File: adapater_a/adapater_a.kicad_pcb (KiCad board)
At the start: 2 copper layers, 68.6 x 53.3 mm, 8 parts, among them J1 Power, J2 Digital/PWM, J3 Analog, J4 Digital/PWM

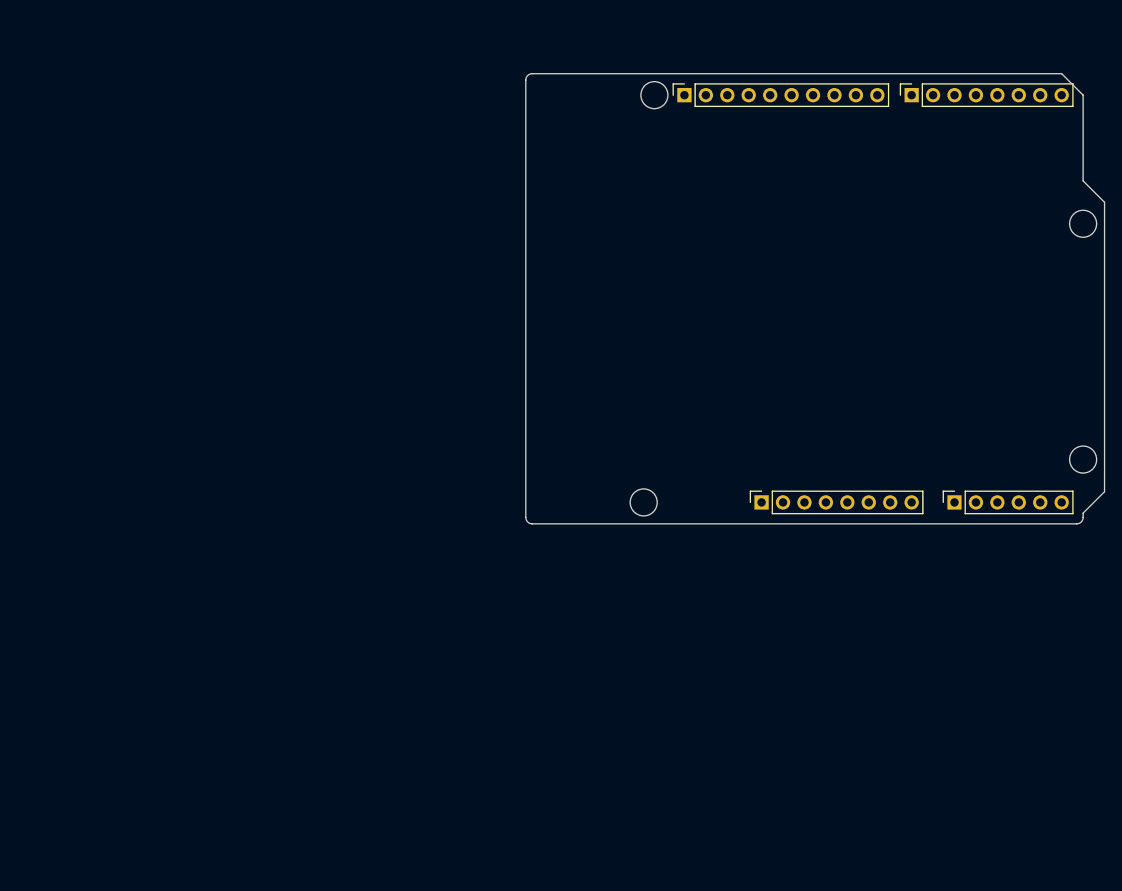
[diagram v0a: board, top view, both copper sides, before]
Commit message: Add first version of adpater A
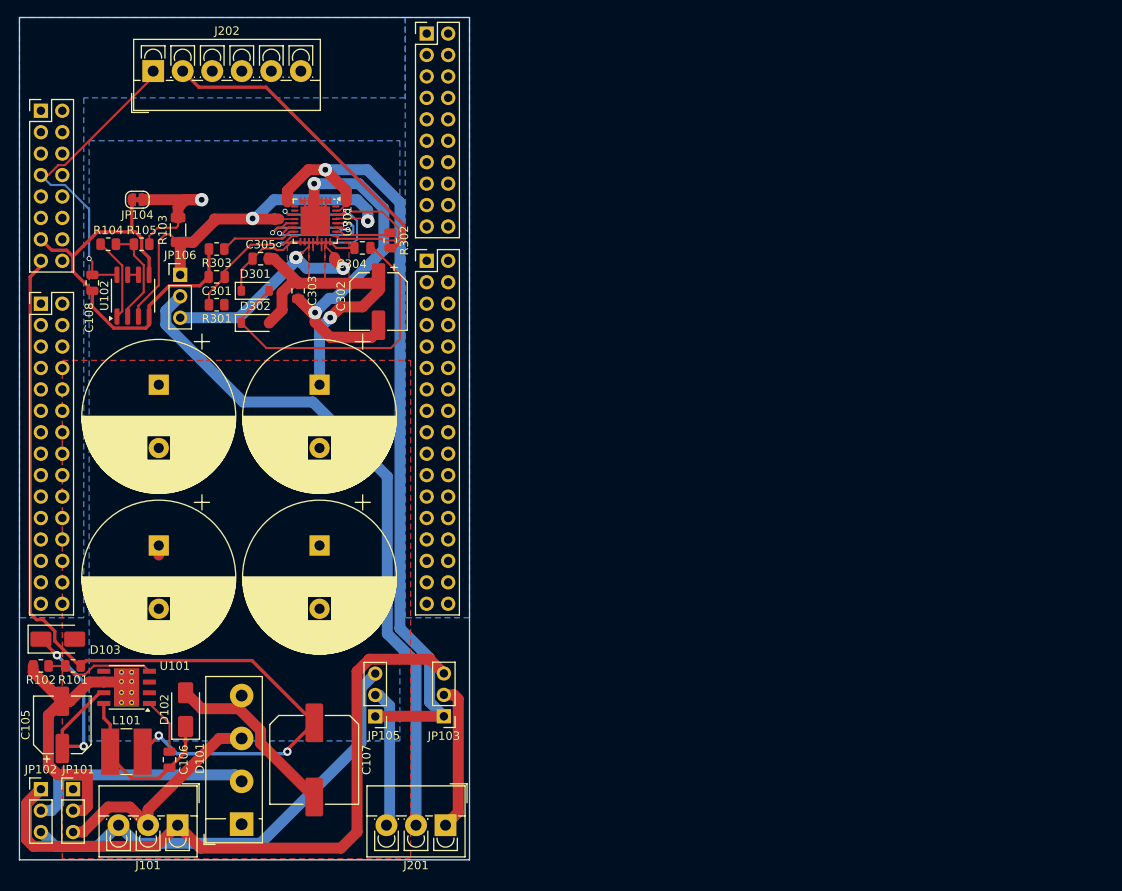
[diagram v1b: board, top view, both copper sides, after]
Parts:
- removed J1: Power, Connector_PinSocket_2.54mm:PinSocket_1x08_P2.54mm_Vertical
- removed J2: Digital/PWM, Connector_PinSocket_2.54mm:PinSocket_1x10_P2.54mm_Vertical
- removed J3: Analog, Connector_PinSocket_2.54mm:PinSocket_1x06_P2.54mm_Vertical
- removed J4: Digital/PWM, Connector_PinSocket_2.54mm:PinSocket_1x08_P2.54mm_Vertical
- removed MH1, MH2, MH3, MH4: MountingHole_3.2mm, Arduino_MountingHole:MountingHole_3.2mm
- added C101: 4m7, Capacitor_THT:CP_Radial_D18.0mm_P7.50mm, F.Cu at (56.5, 102.6)
- added C102: 4m7, Capacitor_THT:CP_Radial_D18.0mm_P7.50mm, F.Cu at (75.6, 102.6)
- added C103: 4m7, Capacitor_THT:CP_Radial_D18.0mm_P7.50mm, F.Cu at (75.6, 83.5)
- added C104: 4m7, Capacitor_THT:CP_Radial_D18.0mm_P7.50mm, F.Cu at (56.5, 83.5)
- added C105: 10u, Capacitor_SMD:CP_Elec_6.3x5.4, F.Cu at (45.1, 123.8)
- added C106: 10n, Capacitor_SMD:C_0805_2012Metric, F.Cu at (57.8, 127.9)
- added C107: 220u, Capacitor_SMD:C_Elec_10x10.2, F.Cu at (74.9, 128.0)
- added C108: 100n, Capacitor_SMD:C_0805_2012Metric, F.Cu at (48.6, 71.4)
- added C301: 5n6, Capacitor_SMD:C_0805_2012Metric, F.Cu at (63.4, 70.7)
- added C302: 100u, Capacitor_SMD:CP_Elec_6.3x5.4, F.Cu at (82.5, 73.7)
- added C303: 100n, Capacitor_SMD:C_0805_2012Metric, F.Cu at (73.0, 72.4)
- added C304: 10n, Capacitor_SMD:C_0805_2012Metric, F.Cu at (80.6, 67.3)
- added C305: 220n, Capacitor_SMD:C_0805_2012Metric, F.Cu at (68.6, 68.6)
- added D101: KBL406, Diode_THT:Diode_Bridge_Vishay_KBL, F.Cu at (66.3, 135.6)
- added D102: B340, Diode_SMD:D_SMA, F.Cu at (59.7, 122.0)
- added D103: B340, Diode_SMD:D_SMA, F.Cu at (44.5, 113.7)
- added D301: 1N4148W, Diode_SMD:D_SOD-123, F.Cu at (67.9, 72.4)
- added D302: 1N4148W, Diode_SMD:D_SOD-123, F.Cu at (67.9, 76.2)
- added J101: Conn_01x03, TerminalBlock_4Ucon:TerminalBlock_4Ucon_1x03_P3.50mm_Vertical, F.Cu at (58.7, 135.7)
- added J102: CN8, Connector_PinHeader_2.54mm:PinHeader_2x08_P2.54mm_Vertical, F.Cu at (42.5, 51.0)
- added J103: CN9, Connector_PinHeader_2.54mm:PinHeader_2x15_P2.54mm_Vertical, F.Cu at (42.5, 73.9)
- added J104: CN7, Connector_PinHeader_2.54mm:PinHeader_2x10_P2.54mm_Vertical, F.Cu at (88.3, 41.9)
- added J105: CN10, Connector_PinHeader_2.54mm:PinHeader_2x17_P2.54mm_Vertical, F.Cu at (88.3, 68.8)
- added J201: Conn_01x03, TerminalBlock_4Ucon:TerminalBlock_4Ucon_1x03_P3.50mm_Vertical, F.Cu at (90.5, 135.7)
- added J202: Conn_01x06, TerminalBlock_4Ucon:TerminalBlock_4Ucon_1x06_P3.50mm_Vertical, F.Cu at (55.8, 46.4)
- added JP101: Jumper_3_Bridged12, Connector_PinHeader_2.54mm:PinHeader_1x03_P2.54mm_Vertical, F.Cu at (46.4, 131.4)
- added JP102: Jumper_3_Bridged12, Connector_PinHeader_2.54mm:PinHeader_1x03_P2.54mm_Vertical, F.Cu at (42.5, 131.4)
- added JP103: Jumper_3_Bridged12, Connector_PinHeader_2.54mm:PinHeader_1x03_P2.54mm_Vertical, F.Cu at (90.3, 122.8)
- added JP104: SolderJumper_2_Bridged, Jumper:SolderJumper-2_P1.3mm_Bridged_RoundedPad1.0x1.5mm, F.Cu at (54.0, 61.6)
- added JP105: Jumper_3_Bridged12, Connector_PinHeader_2.54mm:PinHeader_1x03_P2.54mm_Vertical, F.Cu at (82.2, 122.8)
- added JP106: Jumper_3_Bridged12, Connector_PinHeader_2.54mm:PinHeader_1x03_P2.54mm_Vertical, F.Cu at (59.0, 70.5)
- added L101: 47u, Inductor_SMD:L_Ferrocore_DLG-0504, F.Cu at (52.7, 127.0)
- added R101: 10k, Resistor_SMD:R_0805_2012Metric, F.Cu at (46.4, 116.8)
- added R102: 1k2, Resistor_SMD:R_0805_2012Metric, F.Cu at (42.5, 116.8)
- added R103: 0R1, Resistor_SMD:R_1206_3216Metric, F.Cu at (58.8, 65.2)
- added R104: 68k, Resistor_SMD:R_0805_2012Metric, F.Cu at (50.5, 66.9)
- added R105: 10k, Resistor_SMD:R_0805_2012Metric, F.Cu at (54.5, 66.9)
- added R301: 100k, Resistor_SMD:R_0805_2012Metric, F.Cu at (63.4, 74.0)
- added R302: 5k, Resistor_SMD:R_0805_2012Metric, F.Cu at (83.9, 66.4)
- added R303: 5k, Resistor_SMD:R_0805_2012Metric, F.Cu at (63.4, 67.4)
- added U101: TPS5430DDA, Package_SO:TI_SO-PowerPAD-8_ThermalVias, F.Cu at (52.7, 119.4)
- added U102: TLV2372, Package_SO:SOIC-8_3.9x4.9mm_P1.27mm, F.Cu at (53.5, 73.0)
- added U301: L6226, Package_DFN_QFN:UFQFPN-32-1EP_5x5mm_P0.5mm_EP3.5x3.5mm, F.Cu at (75.1, 64.1)
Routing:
- net GNDPWR: track 0.00 -> 134.2 mm, vias 0 -> 3
- net VCC: track 0.00 -> 105.4 mm, vias 0 -> 2
- net /Driver/V_TRACK: track 0.00 -> 96.0 mm, vias 0 -> 1
- net GND: track 0.00 -> 89.2 mm
- net /V_drive: track 0.00 -> 82.1 mm
- net /Connector/GND_PWR: track 0.00 -> 80.5 mm
- net Net-(U301-ENB): track 0.00 -> 54.5 mm, vias 0 -> 3
- net /V_switch: track 0.00 -> 54.4 mm
- net /Driver/GND_SENSE: track 0.00 -> 52.4 mm, vias 0 -> 2
- net /Driver/V_in: track 0.00 -> 41.1 mm, vias 0 -> 1
- net Net-(D301-A): track 0.00 -> 38.1 mm
- net +3V3: track 0.00 -> 37.0 mm, vias 0 -> 1
- net /Driver/GND_TRACK: track 0.00 -> 30.6 mm, vias 0 -> 2
- net Net-(JP102-C): track 0.00 -> 27.6 mm
- net /GND_PWR: track 0.00 -> 27.4 mm
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- added copper zone on F.Cu, net /Driver/GND_TRACK
- added copper zone on F.Cu, net /Driver/V_in
- added copper zone on B.Cu, net GND
- added copper zone on B.Cu, net GNDPWR
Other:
- board size 68.6 x 53.3 mm -> 53.3 x 99.8 mm
- copper layers 2 -> 4
- board text removed: "ICSP"
